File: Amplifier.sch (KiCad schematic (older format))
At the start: 58 parts, among them J501 TB001-500-04BE CUI_Devices, Q401 2N7002, Q402 2N7002, SW501 DS04-254-2-02BK-SMT, U501 TDA7498L

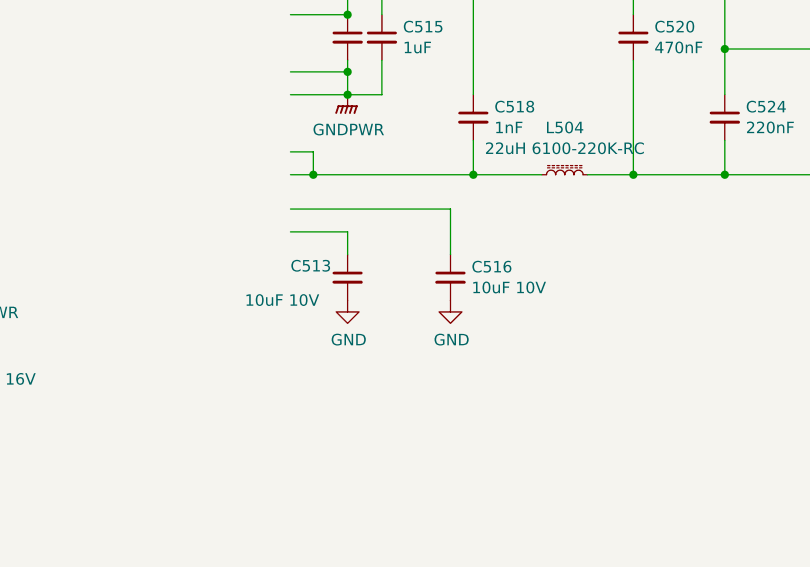
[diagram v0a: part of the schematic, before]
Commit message: 3v3 regler ändern
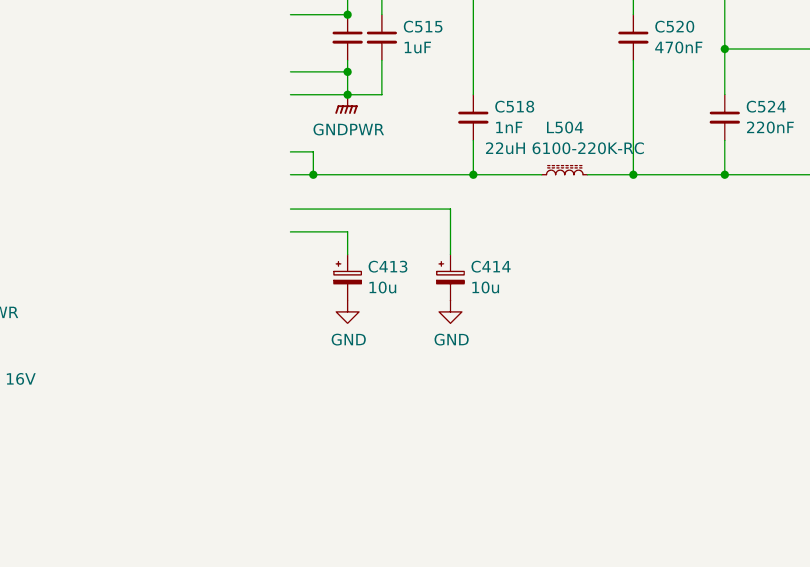
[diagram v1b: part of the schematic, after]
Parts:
- removed C513, C516: 10uF 10V, Capacitor_SMD:C_0603_1608Metric_Pad1.05x0.95mm_HandSolder, symbol Device:C_Small
- added C413, C414: 10u, Capacitor_THT:CP_Radial_D4.0mm_P2.00mm, symbol Device:CP_Small
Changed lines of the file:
@@
 Wire Wire Line
 	6500 3500 6500 4350
-$Comp
-L Device:C_Small C513
-U 1 1 5E79098E
-P 6350 5600
-F 0 "C513" H 6100 5650 50  0000 L CNN
-F 1 "10uF 10V" H 5900 5500 50  0000 L CNN
-F 2 "Capacitor_SMD:C_0603_1608Metric_Pad1.05x0.95mm_HandSolder" H 6350 5600 50  0001 C CNN
-F 3 "~" H 6350 5600 50  0001 C CNN
-	1    6350 5600
-	1    0    0    -1
-$EndComp
-$Comp
-L Device:C_Small C516
-U 1 1 5E7909FE
-P 6800 5600
-F 0 "C516" H 6892 5646 50  0000 L CNN
-F 1 "10uF 10V" H 6892 5555 50  0000 L CNN
-F 2 "Capacitor_SMD:C_0603_1608Metric_Pad1.05x0.95mm_HandSolder" H 6800 5600 50  0001 C CNN
-F 3 "~" H 6800 5600 50  0001 C CNN
-	1    6800 5600
-	1    0    0    -1
-$EndComp
 Wire Wire Line
 	6350 5500 6350 5400
@@
 Wire Wire Line
 	8400 3800 8550 3800
+$Comp
+L Device:CP_Small C413
+U 1 1 5FEA7896
+P 6350 5600
+F 0 "C413" H 6438 5646 50  0000 L CNN
+F 1 "10u" H 6438 5555 50  0000 L CNN
+F 2 "Capacitor_THT:CP_Radial_D4.0mm_P2.00mm" H 6350 5600 50  0001 C CNN
+F 3 "~" H 6350 5600 50  0001 C CNN
+	1    6350 5600
+	1    0    0    -1
+$EndComp
+$Comp
+L Device:CP_Small C414
+U 1 1 5FEA7BCB
+P 6800 5600
+F 0 "C414" H 6888 5646 50  0000 L CNN
+F 1 "10u" H 6888 5555 50  0000 L CNN
+F 2 "Capacitor_THT:CP_Radial_D4.0mm_P2.00mm" H 6800 5600 50  0001 C CNN
+F 3 "~" H 6800 5600 50  0001 C CNN
+	1    6800 5600
+	1    0    0    -1
+$EndComp
 $EndSCHEMATC

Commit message: vor änderungen von der Arbeit
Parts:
- C533, C535: footprint Capacitor_THT:C_Rect_L7.2mm_W7.2mm_P5.00mm_FKS2_FKP2_MKS2_MKP2 -> Capacitor_THT:C_Rect_L7.2mm_W3.5mm_P5.00mm_FKS2_FKP2_MKS2_MKP2
- U501: symbol Amplifier_Audio:TDA7498L -> MukkeBox-rescue:TDA7498L-Amplifier_Audio
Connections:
- wire segments 199 -> 198
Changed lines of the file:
@@
 $EndDescr
 $Comp
-L Amplifier_Audio:TDA7498L U501
+L MukkeBox-rescue:TDA7498L-Amplifier_Audio U501
 U 1 1 5E757365
 P 5400 3650
+AR Path="/5E757365" Ref="U501"  Part="1"
+AR Path="/5E751A81/5E757365" Ref="U501"  Part="1"
 F 0 "U501" H 5425 5415 50  0000 C CNN
 F 1 "TDA7498L" H 5425 5324 50  0000 C CNN
@@
 $EndComp
 Wire Wire Line
-	3250 2750 3050 2750
-Wire Wire Line
 	3000 2500 3000 2750
 Wire Wire Line
@@
 F 0 "C535" V 4150 2100 50  0000 C CNN
 F 1 "1u" V 4050 2150 50  0000 C CNN
-F 2 "Capacitor_THT:C_Rect_L7.2mm_W7.2mm_P5.00mm_FKS2_FKP2_MKS2_MKP2" H 4200 2250 50  0001 C CNN
+F 2 "Capacitor_THT:C_Rect_L7.2mm_W3.5mm_P5.00mm_FKS2_FKP2_MKS2_MKP2" H 4200 2250 50  0001 C CNN
 F 3 "~" H 4200 2250 50  0001 C CNN
 	1    4200 2250
@@
 F 0 "C533" H 4400 5150 50  0000 C CNN
 F 1 "1u" H 4400 5050 50  0000 C CNN
-F 2 "Capacitor_THT:C_Rect_L7.2mm_W7.2mm_P5.00mm_FKS2_FKP2_MKS2_MKP2" H 4200 5150 50  0001 C CNN
+F 2 "Capacitor_THT:C_Rect_L7.2mm_W3.5mm_P5.00mm_FKS2_FKP2_MKS2_MKP2" H 4200 5150 50  0001 C CNN
 F 3 "~" H 4200 5150 50  0001 C CNN
 	1    4200 5150
@@
 	4300 2250 4750 2250
 $Comp
-L power:GND #PWR0413
-U 1 1 5EEA9F5C
-P 6800 5700
-F 0 "#PWR0413" H 6800 5450 50  0001 C CNN
-F 1 "GND" H 6805 5527 50  0000 C CNN
-F 2 "" H 6800 5700 50  0001 C CNN
-F 3 "" H 6800 5700 50  0001 C CNN
-	1    6800 5700
-	1    0    0    -1
-$EndComp
-$Comp
-L power:GND #PWR0412
-U 1 1 5EEAA0E6
-P 6350 5700
-F 0 "#PWR0412" H 6350 5450 50  0001 C CNN
-F 1 "GND" H 6355 5527 50  0000 C CNN
-F 2 "" H 6350 5700 50  0001 C CNN
-F 3 "" H 6350 5700 50  0001 C CNN
-	1    6350 5700
-	1    0    0    -1
-$EndComp
-$Comp
-L power:GND #PWR0411
-U 1 1 5EEB6CAA
-P 4550 6450
-F 0 "#PWR0411" H 4550 6200 50  0001 C CNN
-F 1 "GND" H 4650 6350 50  0000 C CNN
-F 2 "" H 4550 6450 50  0001 C CNN
-F 3 "" H 4550 6450 50  0001 C CNN
-	1    4550 6450
-	1    0    0    -1
-$EndComp
-$Comp
-L power:GND #PWR0410
-U 1 1 5EEB6EFD
-P 4000 6450
-F 0 "#PWR0410" H 4000 6200 50  0001 C CNN
-F 1 "GND" H 4100 6350 50  0000 C CNN
-F 2 "" H 4000 6450 50  0001 C CNN
-F 3 "" H 4000 6450 50  0001 C CNN
-	1    4000 6450
-	1    0    0    -1
-$EndComp
-$Comp
-L power:GND #PWR0408
-U 1 1 5EEB7040
-P 3300 4250
-F 0 "#PWR0408" H 3300 4000 50  0001 C CNN
-F 1 "GND" H 3305 4077 50  0000 C CNN
-F 2 "" H 3300 4250 50  0001 C CNN
-F 3 "" H 3300 4250 50  0001 C CNN
-	1    3300 4250
-	1    0    0    -1
-$EndComp
-Wire Wire Line
-	3150 4250 3300 4250
-Connection ~ 3300 4250
-Wire Wire Line
-	3300 4250 3500 4250
-$Comp
-L power:GND #PWR0405
-U 1 1 5EEB7231
-P 3050 2750
-F 0 "#PWR0405" H 3050 2500 50  0001 C CNN
-F 1 "GND" H 3055 2577 50  0000 C CNN
-F 2 "" H 3050 2750 50  0001 C CNN
-F 3 "" H 3050 2750 50  0001 C CNN
-	1    3050 2750
-	1    0    0    -1
-$EndComp
-Connection ~ 3050 2750
-Wire Wire Line
-	3050 2750 3000 2750
-$Comp
 L power:GND #PWR0414
 U 1 1 5EEB78DA
@@
 	1    0    0    -1
 $EndComp
-Connection ~ 7700 3800
 $Comp
 L power:+3.3V #PWR0401
@@
 Wire Wire Line
 	3550 5700 2500 5700
-$Comp
-L power:GND #PWR0403
-U 1 1 5EF3FD4E
-P 2750 6450
-F 0 "#PWR0403" H 2750 6200 50  0001 C CNN
-F 1 "GND" H 2850 6350 50  0000 C CNN
-F 2 "" H 2750 6450 50  0001 C CNN
-F 3 "" H 2750 6450 50  0001 C CNN
-	1    2750 6450
-	1    0    0    -1
-$EndComp
-$Comp
-L power:GND #PWR0409
-U 1 1 5EF3FDC5
-P 3550 7050
-F 0 "#PWR0409" H 3550 6800 50  0001 C CNN
-F 1 "GND" H 3650 6950 50  0000 C CNN
-F 2 "" H 3550 7050 50  0001 C CNN
-F 3 "" H 3550 7050 50  0001 C CNN
-	1    3550 7050
-	1    0    0    -1
-$EndComp
 Wire Wire Line
 	4550 6450 4550 6100
@@
 Wire Wire Line
 	3050 7050 3550 7050
-Connection ~ 3550 7050
 Wire Wire Line
 	2250 6450 2750 6450
-Connection ~ 2750 6450
 $Comp
 L Device:R_Small R414
@@
 	1    0    0    -1
 $EndComp
+$Comp
+L power:GNDA #PWR0128
+U 1 1 5ED1C814
+P 3000 2750
+F 0 "#PWR0128" H 3000 2500 50  0001 C CNN
+F 1 "GNDA" H 3150 2650 50  0000 C CNN
+F 2 "" H 3000 2750 50  0001 C CNN
+F 3 "" H 3000 2750 50  0001 C CNN
+	1    3000 2750
+	1    0    0    -1
+$EndComp
+Wire Wire Line
+	3000 2750 3250 2750
+Connection ~ 3000 2750
+$Comp
+L power:GNDA #PWR0142
+U 1 1 5ED1C98D
+P 3350 4250
+F 0 "#PWR0142" H 3350 4000 50  0001 C CNN
+F 1 "GNDA" H 3500 4150 50  0000 C CNN
+F 2 "" H 3350 4250 50  0001 C CNN
+F 3 "" H 3350 4250 50  0001 C CNN
+	1    3350 4250
+	1    0    0    -1
+$EndComp
+Wire Wire Line
+	3150 4250 3350 4250
+Connection ~ 3350 4250
+Wire Wire Line
+	3350 4250 3500 4250
+$Comp
+L power:GNDA #PWR0143
+U 1 1 5ED1CBED
+P 6350 5700
+F 0 "#PWR0143" H 6350 5450 50  0001 C CNN
+F 1 "GNDA" H 6500 5600 50  0000 C CNN
+F 2 "" H 6350 5700 50  0001 C CNN
+F 3 "" H 6350 5700 50  0001 C CNN
+	1    6350 5700
+	1    0    0    -1
+$EndComp
+$Comp
+L power:GNDA #PWR0144
+U 1 1 5ED1CF3C
+P 6800 5700
+F 0 "#PWR0144" H 6800 5450 50  0001 C CNN
+F 1 "GNDA" H 6950 5600 50  0000 C CNN
+F 2 "" H 6800 5700 50  0001 C CNN
+F 3 "" H 6800 5700 50  0001 C CNN
+	1    6800 5700
+	1    0    0    -1
+$EndComp
+$Comp
+L power:GNDA #PWR0145
+U 1 1 5ED1CFBB
+P 4550 6450
+F 0 "#PWR0145" H 4550 6200 50  0001 C CNN
+F 1 "GNDA" H 4700 6350 50  0000 C CNN
+F 2 "" H 4550 6450 50  0001 C CNN
+F 3 "" H 4550 6450 50  0001 C CNN
+	1    4550 6450
+	1    0    0    -1
+$EndComp
+$Comp
+L power:GNDA #PWR0146
+U 1 1 5ED1D0F2
+P 4000 6450
+F 0 "#PWR0146" H 4000 6200 50  0001 C CNN
+F 1 "GNDA" H 4150 6350 50  0000 C CNN
+F 2 "" H 4000 6450 50  0001 C CNN
+F 3 "" H 4000 6450 50  0001 C CNN
+	1    4000 6450
+	1    0    0    -1
+$EndComp
+$Comp
+L power:GNDA #PWR0152
+U 1 1 5ED1D1E5
+P 2750 6450
+F 0 "#PWR0152" H 2750 6200 50  0001 C CNN
+F 1 "GNDA" H 2900 6350 50  0000 C CNN
+F 2 "" H 2750 6450 50  0001 C CNN
+F 3 "" H 2750 6450 50  0001 C CNN
+	1    2750 6450
+	1    0    0    -1
+$EndComp
+$Comp
+L power:GNDA #PWR0153
+U 1 1 5ED1D264
+P 3550 7050
+F 0 "#PWR0153" H 3550 6800 50  0001 C CNN
+F 1 "GNDA" H 3700 6950 50  0000 C CNN
+F 2 "" H 3550 7050 50  0001 C CNN
+F 3 "" H 3550 7050 50  0001 C CNN
+	1    3550 7050
+	1    0    0    -1
+$EndComp
+Connection ~ 2750 6450
+Connection ~ 3550 7050
 $EndSCHEMATC

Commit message: Nach Änderungen auf der Arbeit + anderes
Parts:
- added R4, R5: 0R, Resistor_SMD:R_1206_3216Metric_Pad1.42x1.75mm_HandSolder, symbol Device:R_Small
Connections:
- net GND: now also R4.2, R5.2
- net GNDPWR: now also R4.1, R5.1
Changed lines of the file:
@@
 U 1 1 5EC064F0
 P 8000 3800
-F 0 "R512" V 7804 3800 50  0000 C CNN
-F 1 "0R" V 7895 3800 50  0000 C CNN
+F 0 "R512" V 7900 3550 50  0000 C CNN
+F 1 "0R" V 7950 3550 50  0000 C CNN
 F 2 "Resistor_SMD:R_1206_3216Metric_Pad1.42x1.75mm_HandSolder" H 8000 3800 50  0001 C CNN
 F 3 "~" H 8000 3800 50  0001 C CNN
@@
 $EndComp
 Wire Wire Line
-	8100 3800 8250 3800
+	8100 3800 8150 3800
 $Comp
 L power:PWR_FLAG #FLG0111
@@
 $EndComp
 Wire Wire Line
-	7700 3800 7900 3800
+	7700 3800 7850 3800
 $Comp
 L Device:CP_Small C525
@@
 Connection ~ 2750 6450
 Connection ~ 3550 7050
+$Comp
+L Device:R_Small R5
+U 1 1 5ED99689
+P 8000 3900
+F 0 "R5" V 7950 4100 50  0000 C CNN
+F 1 "0R" V 8050 4100 50  0000 C CNN
+F 2 "Resistor_SMD:R_1206_3216Metric_Pad1.42x1.75mm_HandSolder" H 8000 3900 50  0001 C CNN
+F 3 "~" H 8000 3900 50  0001 C CNN
+	1    8000 3900
+	0    1    1    0
+$EndComp
+$Comp
+L Device:R_Small R4
+U 1 1 5ED99910
+P 8000 3700
+F 0 "R4" V 7900 3700 50  0000 C CNN
+F 1 "0R" V 7950 3700 50  0000 C CNN
+F 2 "Resistor_SMD:R_1206_3216Metric_Pad1.42x1.75mm_HandSolder" H 8000 3700 50  0001 C CNN
+F 3 "~" H 8000 3700 50  0001 C CNN
+	1    8000 3700
+	0    1    1    0
+$EndComp
+Wire Wire Line
+	8100 3700 8150 3700
+Wire Wire Line
+	8150 3700 8150 3800
+Connection ~ 8150 3800
+Wire Wire Line
+	8150 3800 8250 3800
+Wire Wire Line
+	8100 3900 8150 3900
+Wire Wire Line
+	8150 3900 8150 3800
+Wire Wire Line
+	7900 3700 7850 3700
+Wire Wire Line
+	7850 3700 7850 3800
+Connection ~ 7850 3800
+Wire Wire Line
+	7850 3800 7900 3800
+Wire Wire Line
+	7900 3900 7850 3900
+Wire Wire Line
+	7850 3900 7850 3800
 $EndSCHEMATC
